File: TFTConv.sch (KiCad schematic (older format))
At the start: 2 parts, among them J1 Board, J2 Screen

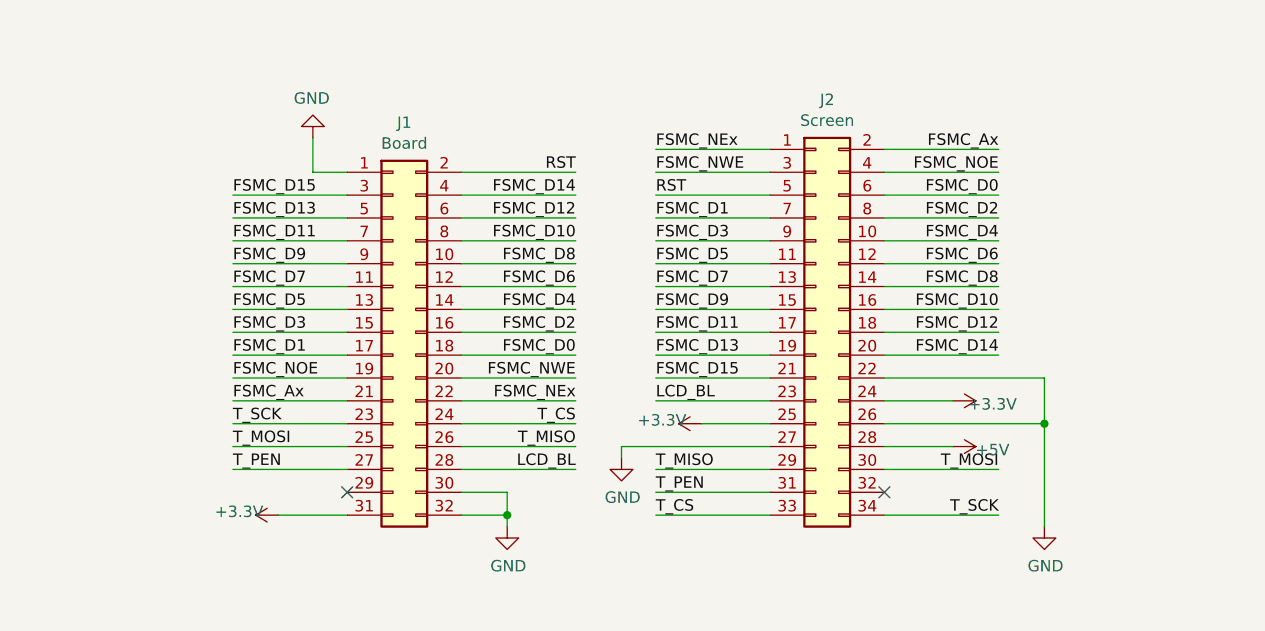
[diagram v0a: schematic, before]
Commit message: TFTConv: PCB finished
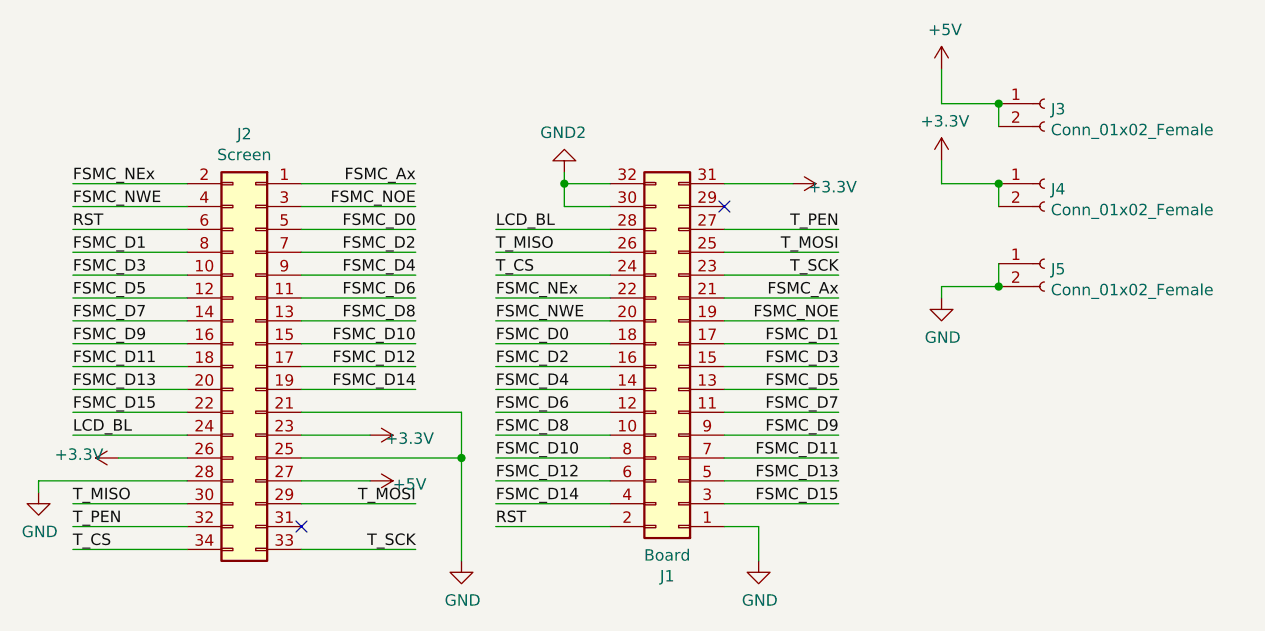
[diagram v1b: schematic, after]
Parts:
- added J3, J4, J5: Conn_01x02_Female, Connector_PinSocket_2.54mm:PinSocket_1x02_P2.54mm_Vertical, symbol Connector:Conn_01x02_Female
- J1: footprint (none) -> Connector_PinSocket_2.54mm:PinSocket_2x16_P2.54mm_Vertical
- J2: footprint (none) -> Connector_PinSocket_2.54mm:PinSocket_2x17_P2.54mm_Vertical
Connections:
- net +3V3: now also J2.23 (Pin_23), J2.26 (Pin_26), J4.1 (Pin_1), J4.2 (Pin_2); no longer J2.24 (Pin_24), J2.25 (Pin_25)
- net +5V: now also J2.27 (Pin_27), J3.1 (Pin_1), J3.2 (Pin_2); no longer J2.28 (Pin_28)
- net FSMC_Ax: now also J2.1 (Pin_1); no longer J2.2 (Pin_2)
- net FSMC_D0: now also J2.5 (Pin_5); no longer J2.6 (Pin_6)
- net FSMC_D1: now also J2.8 (Pin_8); no longer J2.7 (Pin_7)
- net FSMC_D10: now also J2.15 (Pin_15); no longer J2.16 (Pin_16)
- net FSMC_D11: now also J2.18 (Pin_18); no longer J2.17 (Pin_17)
- net FSMC_D12: now also J2.17 (Pin_17); no longer J2.18 (Pin_18)
- net FSMC_D13: now also J2.20 (Pin_20); no longer J2.19 (Pin_19)
- net FSMC_D14: now also J2.19 (Pin_19); no longer J2.20 (Pin_20)
- net FSMC_D15: now also J2.22 (Pin_22); no longer J2.21 (Pin_21)
- net FSMC_D2: now also J2.7 (Pin_7); no longer J2.8 (Pin_8)
- net FSMC_D3: now also J2.10 (Pin_10); no longer J2.9 (Pin_9)
- net FSMC_D4: now also J2.9 (Pin_9); no longer J2.10 (Pin_10)
- net FSMC_D5: now also J2.12 (Pin_12); no longer J2.11 (Pin_11)
- net FSMC_D6: now also J2.11 (Pin_11); no longer J2.12 (Pin_12)
- net FSMC_D7: now also J2.14 (Pin_14); no longer J2.13 (Pin_13)
- net FSMC_D8: now also J2.13 (Pin_13); no longer J2.14 (Pin_14)
- net FSMC_D9: now also J2.16 (Pin_16); no longer J2.15 (Pin_15)
- net FSMC_NEx: now also J2.2 (Pin_2); no longer J2.1 (Pin_1)
- net FSMC_NOE: now also J2.3 (Pin_3); no longer J2.4 (Pin_4)
- net FSMC_NWE: now also J2.4 (Pin_4); no longer J2.3 (Pin_3)
- net GND: now also J2.21 (Pin_21), J2.25 (Pin_25), J2.28 (Pin_28), J5.1 (Pin_1), J5.2 (Pin_2); no longer J1.30 (Pin_30), J1.32 (Pin_32), J2.22 (Pin_22), J2.26 (Pin_26), J2.27 (Pin_27)
- net LCD_BL: now also J2.24 (Pin_24); no longer J2.23 (Pin_23)
- net RST: now also J2.6 (Pin_6); no longer J2.5 (Pin_5)
- net T_CS: now also J2.34 (Pin_34); no longer J2.33 (Pin_33)
- net T_MISO: now also J2.30 (Pin_30); no longer J2.29 (Pin_29)
- net T_MOSI: now also J2.29 (Pin_29); no longer J2.30 (Pin_30)
- net T_PEN: now also J2.32 (Pin_32); no longer J2.31 (Pin_31)
- net T_SCK: now also J2.33 (Pin_33); no longer J2.34 (Pin_34)
- new net GND2: J1.30 (Pin_30), J1.32 (Pin_32)
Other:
- moved on the sheet: J1, J2
